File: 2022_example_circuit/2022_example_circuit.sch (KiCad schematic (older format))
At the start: 12 parts, among them Q1 IRFS4115, U1 OKI, U2 LT1910

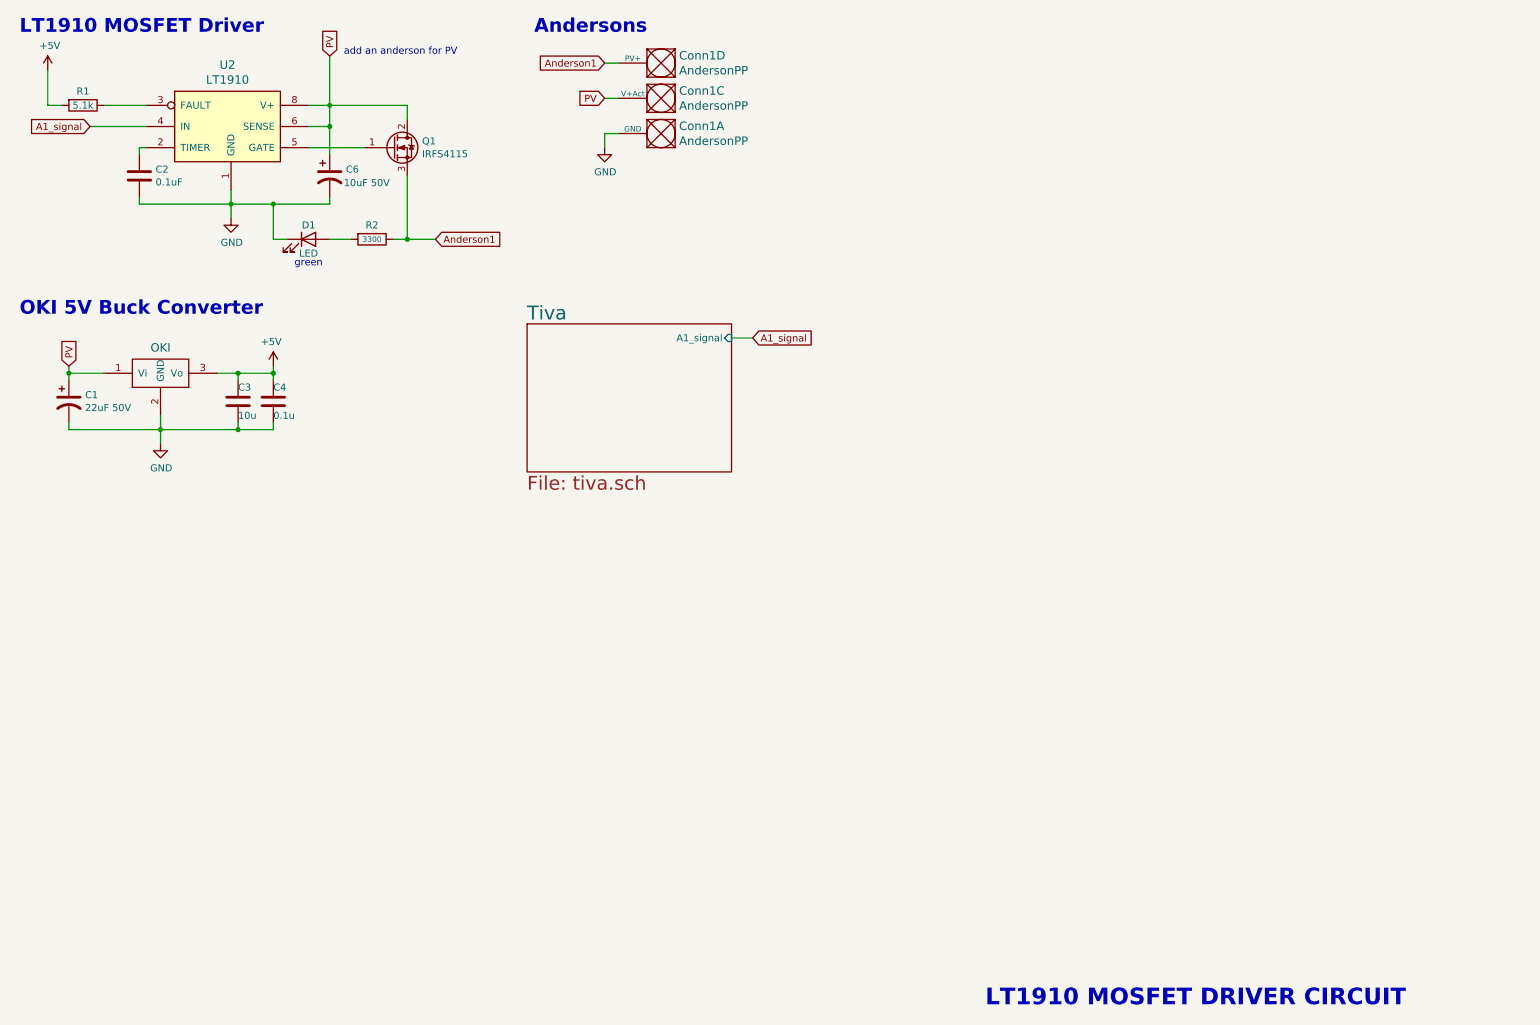
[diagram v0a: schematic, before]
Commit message: Created Schematic for Training Hardware
Schematic for:
LT1910 MOSFET Driver
Andersons
5V Buck Converter
3V3 Buck Converter
Tiva (hierarchical sheet)
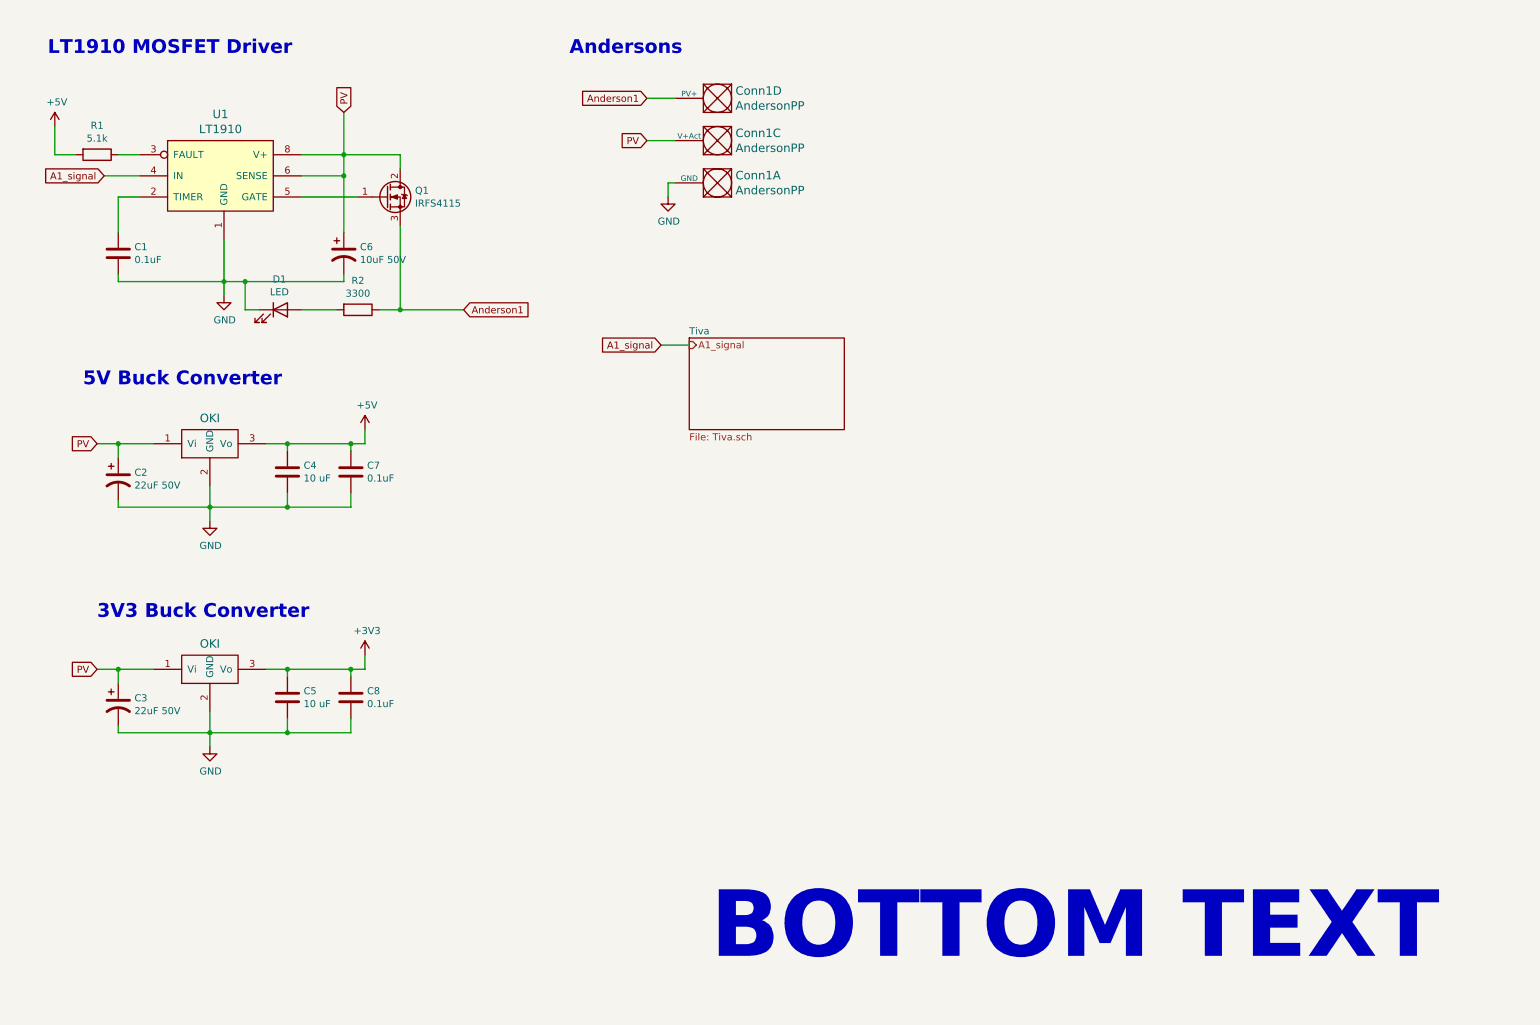
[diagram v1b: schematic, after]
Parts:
- removed C1: 22uF 50V, Capacitor_THT:CP_Radial_D6.3mm_P2.50mm, symbol Device:CP1
- removed C2: 0.1uF, Capacitor_SMD:C_0603_1608Metric_Pad1.08x0.95mm_HandSolder, symbol Device:C
- removed C3: 10u, Capacitor_SMD:C_0603_1608Metric_Pad1.08x0.95mm_HandSolder, symbol Device:C
- removed U1: OKI, MRDT_Devices:OKI_Horizontal, symbol MRDT_Devices:OKI
- removed U2: LT1910, Package_SO:SOIC-8_3.9x4.9mm_P1.27mm, symbol MRDT_ICs:LT1910
- added C1, C7, C8: 0.1uF, symbol Device:C
- added C2, C3: 22uF 50V, symbol Device:CP1
- added C5: 10 uF, symbol Device:C
- added U1: LT1910, symbol MRDT_ICs:LT1910
- added U2, U3: OKI, symbol MRDT_Devices:OKI
- C4: value 0.1u -> 10 uF; footprint Capacitor_SMD:C_0603_1608Metric_Pad1.08x0.95mm_HandSolder -> (none)
- C6: footprint Capacitor_THT:CP_Radial_D6.3mm_P2.50mm -> (none)
- Conn1: footprint MRDT_Connectors:Anderson_3_Horizontal_Side_by_Side -> (none)
- D1: footprint LED_SMD:LED_0603_1608Metric_Pad1.05x0.95mm_HandSolder -> (none)
- R1, R2: footprint Resistor_SMD:R_0603_1608Metric_Pad0.98x0.95mm_HandSolder -> (none)
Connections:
- net +5V: now also C7.1, U2.3 (Vo)
- net A1_signal: now also U1.4 (IN)
- net GND: now also C1.2, C2.2, C3.2, C5.2, C7.2, C8.2, U1.1 (GND), U2.2 (GND), U3.2 (GND)
- net PV: now also C2.1, C3.1, U1.6 (SENSE), U1.8 (V+), U2.1 (Vi), U3.1 (Vi)
- net at R1.1: now also U1.3 (FAULT)
- net at Q1.1 (G): now also U1.5 (GATE)
- new net: C1.1, U1.2 (TIMER)
- new net +3V3: C5.1, C8.1, U3.3 (Vo)
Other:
- note added: "3V3 Buck Converter"
- note added: "5V Buck Converter"
- note added: "BOTTOM TEXT"
- note removed: "LT1910 MOSFET DRIVER CIRCUIT"
- note removed: "OKI 5V Buck Converter"
- note removed: "add an anderson for PV"
- note removed: "green"
